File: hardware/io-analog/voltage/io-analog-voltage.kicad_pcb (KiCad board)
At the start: 2 copper layers, 68.6 x 53.3 mm, 20 parts, among them J1 Input

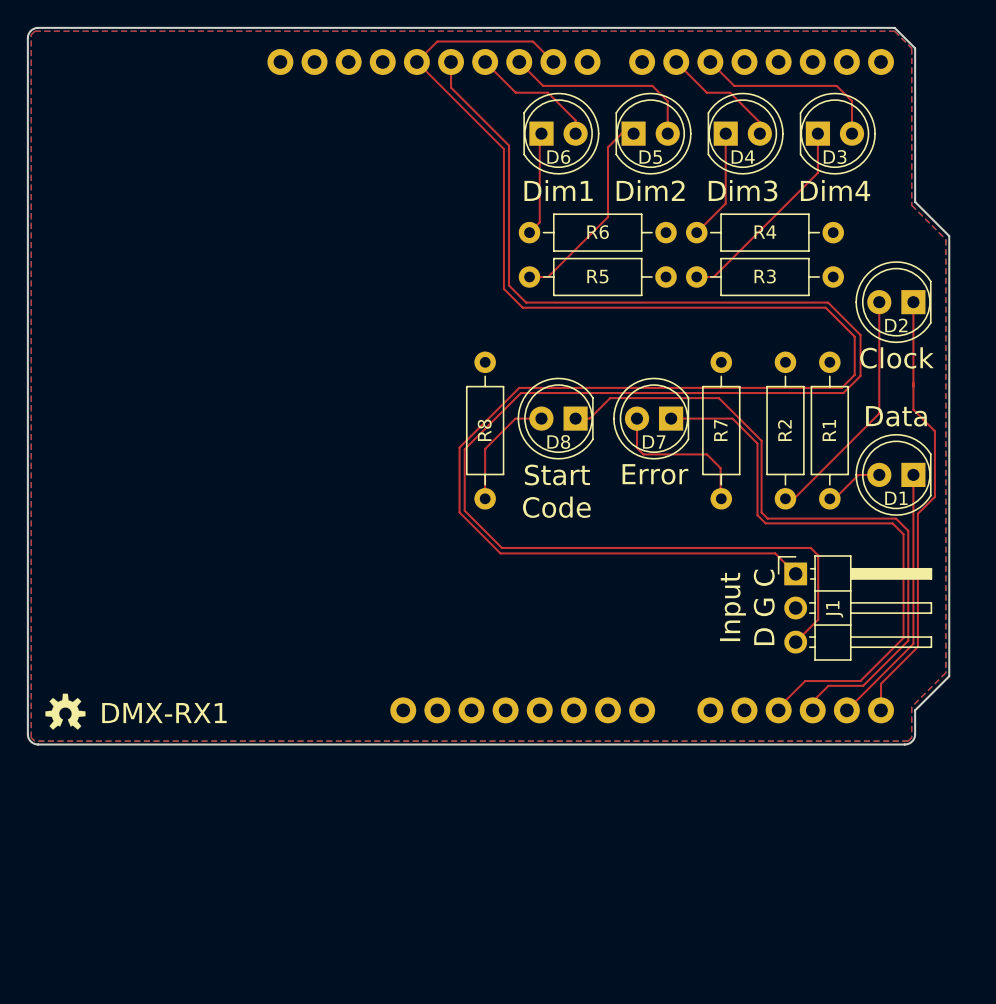
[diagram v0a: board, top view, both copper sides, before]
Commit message: Prototype version of DMX, Analog, and PWM IO Modules and both TX and RX IO interfaces.
Make io-analog a stackable family
io-analog-core handles D to A
io-analog-voltage handles voltage output
io-analog-pwm handles pwm output for leds, drive display pro

Refactor display-pro to work with io-analog-pwm
Add correct coax power connector

Move TX2 to tx-io
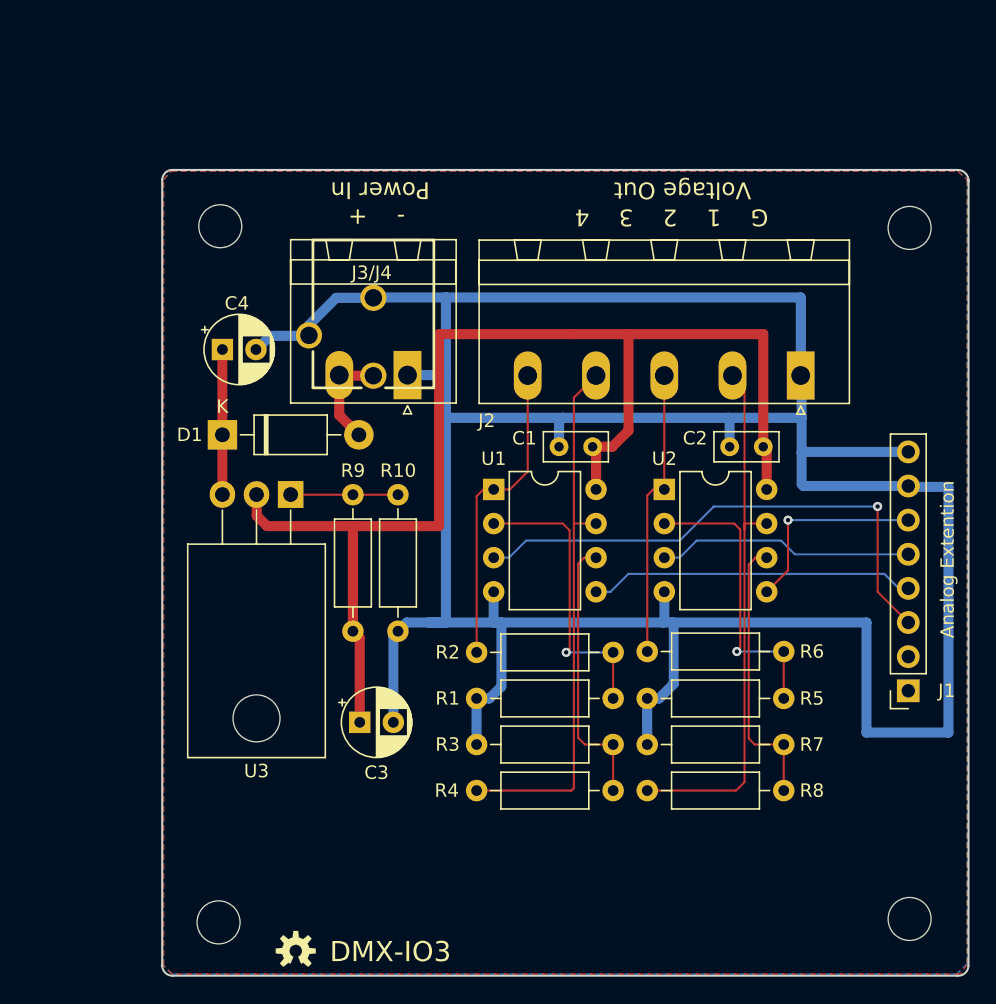
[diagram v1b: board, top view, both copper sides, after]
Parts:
- removed A1: Arduino_UNO_R3, footprints:ARDUINO_R3_NO_HOLES
- removed D2: CLOCK, LED_THT:LED_D5.0mm
- removed D3: DIM3, LED_THT:LED_D5.0mm
- removed D4: DIM2, LED_THT:LED_D5.0mm
- removed D5: DIM1, LED_THT:LED_D5.0mm
- removed D6: DIM0, LED_THT:LED_D5.0mm
- removed D7: ERROR, LED_THT:LED_D5.0mm
- removed D8: START_CODE, LED_THT:LED_D5.0mm
- added C1: 0.1uF, Capacitor_THT:C_Rect_L4.6mm_W2.0mm_P2.50mm_MKS02_FKP02, F.Cu at (158.4, 94.4)
- added C2: 0.1uF, Capacitor_THT:C_Rect_L4.6mm_W2.0mm_P2.50mm_MKS02_FKP02, F.Cu at (171.1, 94.4)
- added C3: 10uF, Capacitor_THT:CP_Radial_D5.0mm_P2.50mm, F.Cu at (141.0, 114.9)
- added C4: 10uF, Capacitor_THT:CP_Radial_D5.0mm_P2.50mm, F.Cu at (130.8, 87.2)
- added J2: Output, Connector_Phoenix_MSTB:PhoenixContact_MSTBA_2,5_5-G-5,08_1x05_P5.08mm_Horizontal, F.Cu at (173.9, 89.1)
- added J3: Power, Connector_Phoenix_MSTB:PhoenixContact_MSTBA_2,5_2-G-5,08_1x02_P5.08mm_Horizontal, F.Cu at (144.6, 89.1)
- added J4: Power, Connectors:POWER_JACK_PTH_BREAD, F.Cu at (142.0, 75.4)
- added MH1: MountingHole, MountingHole:MountingHole_3.2mm_M3, F.Cu at (130.7, 78.0)
- added MH2: MountingHole, MountingHole:MountingHole_3.2mm_M3, F.Cu at (182.0, 78.1)
- added MH3: MountingHole, MountingHole:MountingHole_3.2mm_M3, F.Cu at (130.5, 129.8)
- added MH4: MountingHole, MountingHole:MountingHole_3.2mm_M3, F.Cu at (182.0, 129.6)
- added R10: 2.74k 1%, Resistor_THT:R_Axial_DIN0207_L6.3mm_D2.5mm_P10.16mm_Horizontal, F.Cu at (143.9, 108.2)
- added R9: 392 1%, Resistor_THT:R_Axial_DIN0207_L6.3mm_D2.5mm_P10.16mm_Horizontal, F.Cu at (140.5, 98.0)
- added U1: TLV2772, Package_DIP:DIP-8_W7.62mm, F.Cu at (151.0, 97.6)
- added U2: TLV2772, Package_DIP:DIP-8_W7.62mm, F.Cu at (163.7, 97.6)
- added U3: LM317T, Package_TO_SOT_THT:TO-220-3_Horizontal_TabDown, F.Cu at (135.9, 98.0)
- D1: value DATA -> 1N5819; footprint LED_THT:LED_D5.0mm -> Diode_THT:D_DO-41_SOD81_P10.16mm_Horizontal
- J1: value Input -> Analog Extension; footprint Connector_PinHeader_2.54mm:PinHeader_1x03_P2.54mm_Horizontal -> Connector_PinSocket_2.54mm:PinSocket_1x08_P2.54mm_Vertical
- R1, R3, R5, R7: value 330 -> 22.6k 1%
- R2, R4, R6, R8: value 330 -> 68.1k 1%
- moved D1 51.5 mm to (130.8, 93.5), turned to 0 degrees
- moved R4 44.6 mm to (159.9, 120.0)
- moved R3 43.8 mm to (149.7, 116.6), turned to 0 degrees
- moved R8 38.9 mm to (172.6, 120.0), turned to 180 degrees
- moved R1 36.3 mm to (149.7, 113.2), turned to 0 degrees
- moved R6 32.4 mm to (172.6, 109.7)
- moved R2 31.5 mm to (149.7, 109.7), turned to 0 degrees
- moved R5 31.4 mm to (162.4, 113.2), turned to 0 degrees
- moved R7 29.0 mm to (162.4, 116.6), turned to 0 degrees
- moved G*** 26.1 mm to (137.1, 129.3)
- moved ? 24.6 mm to (136.3, 132.0)
- moved J1 12.1 mm to (181.9, 112.6), turned to 180 degrees
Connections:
- D1 pad 1: /~DATA -> Net-(C4-Pad1)
- J1 pad 1: /RXCLK -> Net-(J1-Pad1)
- J1 pad 2: GND -> Net-(J1-Pad2)
- J1 pad 3: /RX -> /AO3
- R1 pad 1: +5V -> GND
- R1 pad 2: Net-(D1-Pad2) -> Net-(R1-Pad2)
- R2 pad 1: +5V -> Net-(J2-Pad5)
- R2 pad 2: Net-(D2-Pad2) -> Net-(R1-Pad2)
- R3 pad 2: Net-(D3-Pad1) -> Net-(R3-Pad2)
- R4 pad 1: GND -> Net-(R3-Pad2)
- R5 pad 2: Net-(D5-Pad1) -> Net-(R5-Pad2)
- R6 pad 1: GND -> Net-(R5-Pad2)
- R7 pad 1: +5V -> GND
- R7 pad 2: Net-(D7-Pad2) -> Net-(R7-Pad2)
- R8 pad 1: +5V -> Net-(R7-Pad2)
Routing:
- net GND: track 0.00 -> 235.2 mm
- net /RXCLK: track 126.2 -> 0.00 mm
- net /RX: track 120.3 -> 0.00 mm
- net Net-(C1-Pad1): track 0.00 -> 94.3 mm
- net /~SC: track 50.4 -> 0.00 mm
- net /~ERR: track 43.4 -> 0.00 mm
- net /AO3: track 0.00 -> 39.7 mm, vias 0 -> 1
- net /~CLOCK: track 33.0 -> 0.00 mm
- net Net-(J2-Pad4): track 8.26 -> 40.4 mm
- net Net-(J2-Pad2): track 8.84 -> 40.2 mm
- net /AO2: track 0.00 -> 24.2 mm
- net Net-(J2-Pad5): track 0.00 -> 23.5 mm
- net Net-(R5-Pad2): track 0.00 -> 22.0 mm, vias 0 -> 1
- net Net-(R1-Pad2): track 0.00 -> 22.0 mm, vias 0 -> 1
- net Net-(R7-Pad2): track 0.00 -> 20.7 mm
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- added copper zone on F.Cu, net Net-(C1-Pad1)
- removed copper zone on F.Cu, net +5V
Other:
- board size 68.6 x 53.3 mm -> 60 x 60 mm
- net class Power: clearance 0.1524 -> 0.25; trace_width 0.3048 -> 0.75
- board text added: "- + Power In"
- board text added: "Analog Extention"
- board text added: "DMX-IO3"
- board text added: "DMX-IO3, Rev 1.2 Crazy Giraffe Software"
- board text added: "G 1 2 3 4 Voltage Out"
- board text added: "J3/J4"
- board text removed: "Clock"
- board text removed: "D G C"
- board text removed: "DMX-RX1"
- board text removed: "DMX-RX1, Rev 1.3 Crazy Giraffe Software"
- board text removed: "Data"
- board text removed: "Dim1"
- board text removed: "Dim2"
- board text removed: "Dim3"
- board text removed: "Dim4"
- board text removed: "Error"
- board text removed: "Input"
- board text removed: "Start Code"
